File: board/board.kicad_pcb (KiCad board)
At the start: 2 copper layers, 4 parts, among them P2 CONN28

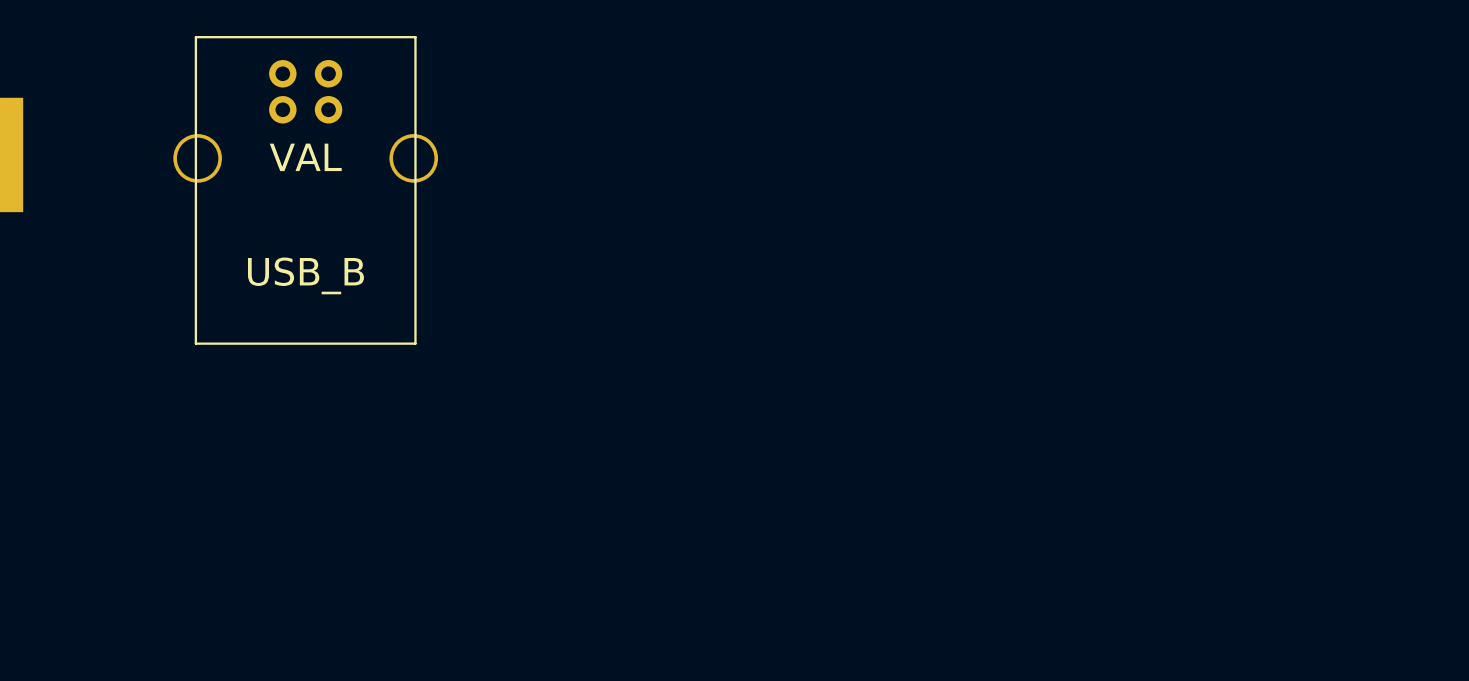
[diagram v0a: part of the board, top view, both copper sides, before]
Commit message: Added some more component outlines.
git-svn-id: http://www.cdkersey.com/log/2015.08.21/eeprom_prog@1664 816618ff-971e-4f3c-9917-b646dc1eeecf
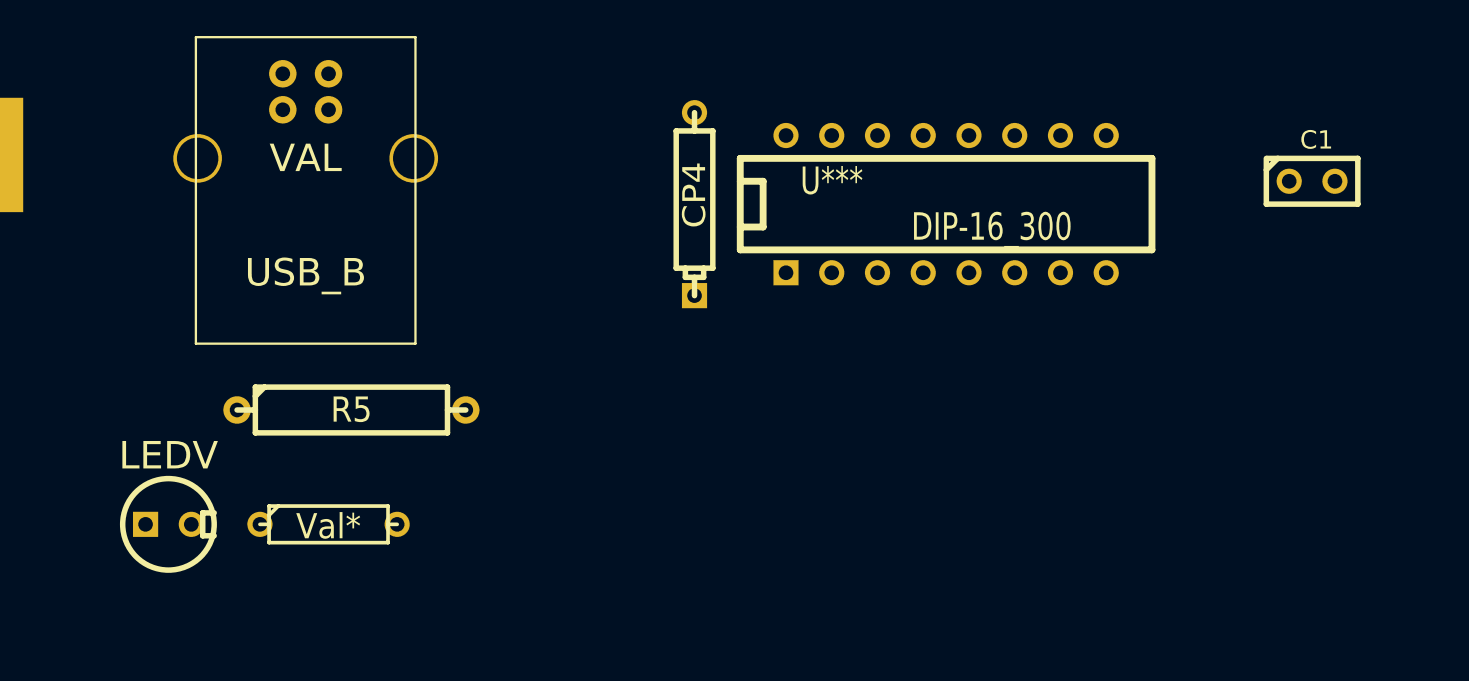
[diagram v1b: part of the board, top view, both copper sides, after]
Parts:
- added C1: V***, C1, F.Cu at (209.6, 77.5)
- added CP4: C***, CP4, F.Cu at (175.3, 78.7)
- added LEDV: D***, LEDV, F.Cu at (146.1, 96.5)
- added R3: Val*, R3, F.Cu at (154.9, 96.5)
- added R5: Val*, R5, F.Cu at (156.2, 90.2)
- added U***: DIP-16_300, DIP-16__300, F.Cu at (189.2, 78.7)
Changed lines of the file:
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@@
     (links 0)
     (no_connects 0)
-    (area 70.616 107.620999 236.549001 180.669001)
+    (area 70.616 69.151499 236.549001 180.669001)
     (thickness 1.6)
     (drawings 0)
     (tracks 0)
     (zones 0)
-    (modules 4)
+    (modules 10)
     (nets 1)
   )
@@
       (rotate (xyz 0 0 0))
     )
+  )
+  (module DIP-16__300 (layer F.Cu)
+    (at 189.23 78.74)
+    (descr "16 pins DIL package, round pads")
+    (tags DIL)
+    (fp_text reference U*** (at -6.35 -1.27) (layer F.SilkS)
+      (effects (font (size 1.524 1.143) (thickness 0.3048)))
+    )
+    (fp_text value DIP-16_300 (at 2.54 1.27) (layer F.SilkS)
+      (effects (font (size 1.524 1.143) (thickness 0.3048)))
+    )
+    (fp_line (start -11.43 -1.27) (end -11.43 -1.27) (layer F.SilkS) (width 0.381))
+    (fp_line (start -11.43 -1.27) (end -10.16 -1.27) (layer F.SilkS) (width 0.381))
+    (fp_line (start -10.16 -1.27) (end -10.16 1.27) (layer F.SilkS) (width 0.381))
+    (fp_line (start -10.16 1.27) (end -11.43 1.27) (layer F.SilkS) (width 0.381))
+    (fp_line (start -11.43 -2.54) (end 11.43 -2.54) (layer F.SilkS) (width 0.381))
+    (fp_line (start 11.43 -2.54) (end 11.43 2.54) (layer F.SilkS) (width 0.381))
+    (fp_line (start 11.43 2.54) (end -11.43 2.54) (layer F.SilkS) (width 0.381))
+    (fp_line (start -11.43 2.54) (end -11.43 -2.54) (layer F.SilkS) (width 0.381))
+    (pad 1 thru_hole rect (at -8.89 3.81) (size 1.397 1.397) (drill 0.8128)
+      (layers *.Cu *.Mask F.SilkS)
+    )
+    (pad 2 thru_hole circle (at -6.35 3.81) (size 1.397 1.397) (drill 0.8128)
+      (layers *.Cu *.Mask F.SilkS)
+    )
+    (pad 3 thru_hole circle (at -3.81 3.81) (size 1.397 1.397) (drill 0.8128)
+      (layers *.Cu *.Mask F.SilkS)
+    )
+    (pad 4 thru_hole circle (at -1.27 3.81) (size 1.397 1.397) (drill 0.8128)
+      (layers *.Cu *.Mask F.SilkS)
+    )
+    (pad 5 thru_hole circle (at 1.27 3.81) (size 1.397 1.397) (drill 0.8128)
+      (layers *.Cu *.Mask F.SilkS)
+    )
+    (pad 6 thru_hole circle (at 3.81 3.81) (size 1.397 1.397) (drill 0.8128)
+      (layers *.Cu *.Mask F.SilkS)
+    )
+    (pad 7 thru_hole circle (at 6.35 3.81) (size 1.397 1.397) (drill 0.8128)
+      (layers *.Cu *.Mask F.SilkS)
+    )
+    (pad 8 thru_hole circle (at 8.89 3.81) (size 1.397 1.397) (drill 0.8128)
+      (layers *.Cu *.Mask F.SilkS)
+    )
+    (pad 9 thru_hole circle (at 8.89 -3.81) (size 1.397 1.397) (drill 0.8128)
+      (layers *.Cu *.Mask F.SilkS)
+    )
+    (pad 10 thru_hole circle (at 6.35 -3.81) (size 1.397 1.397) (drill 0.8128)
+      (layers *.Cu *.Mask F.SilkS)
+    )
+    (pad 11 thru_hole circle (at 3.81 -3.81) (size 1.397 1.397) (drill 0.8128)
+      (layers *.Cu *.Mask F.SilkS)
+    )
+    (pad 12 thru_hole circle (at 1.27 -3.81) (size 1.397 1.397) (drill 0.8128)
+      (layers *.Cu *.Mask F.SilkS)
+    )
+    (pad 13 thru_hole circle (at -1.27 -3.81) (size 1.397 1.397) (drill 0.8128)
+      (layers *.Cu *.Mask F.SilkS)
+    )
+    (pad 14 thru_hole circle (at -3.81 -3.81) (size 1.397 1.397) (drill 0.8128)
+      (layers *.Cu *.Mask F.SilkS)
+    )
+    (pad 15 thru_hole circle (at -6.35 -3.81) (size 1.397 1.397) (drill 0.8128)
+      (layers *.Cu *.Mask F.SilkS)
+    )
+    (pad 16 thru_hole circle (at -8.89 -3.81) (size 1.397 1.397) (drill 0.8128)
+      (layers *.Cu *.Mask F.SilkS)
+    )
+    (model dil/dil_16.wrl
+      (at (xyz 0 0 0))
+      (scale (xyz 1 1 1))
+      (rotate (xyz 0 0 0))
+    )
+  )
+  (module C1 (layer F.Cu)
+    (at 209.55 77.47)
+    (descr "Condensateur e = 1 pas")
+    (tags C)
+    (fp_text reference C1 (at 0.254 -2.286) (layer F.SilkS)
+      (effects (font (size 1.016 1.016) (thickness 0.2032)))
+    )
+    (fp_text value V*** (at 0 -2.286) (layer F.SilkS) hide
+      (effects (font (size 1.016 1.016) (thickness 0.2032)))
+    )
+    (fp_line (start -2.4892 -1.27) (end 2.54 -1.27) (layer F.SilkS) (width 0.3048))
+    (fp_line (start 2.54 -1.27) (end 2.54 1.27) (layer F.SilkS) (width 0.3048))
+    (fp_line (start 2.54 1.27) (end -2.54 1.27) (layer F.SilkS) (width 0.3048))
+    (fp_line (start -2.54 1.27) (end -2.54 -1.27) (layer F.SilkS) (width 0.3048))
+    (fp_line (start -2.54 -0.635) (end -1.905 -1.27) (layer F.SilkS) (width 0.3048))
+    (pad 1 thru_hole circle (at -1.27 0) (size 1.397 1.397) (drill 0.8128)
+      (layers *.Cu *.Mask F.SilkS)
+    )
+    (pad 2 thru_hole circle (at 1.27 0) (size 1.397 1.397) (drill 0.8128)
+      (layers *.Cu *.Mask F.SilkS)
+    )
+    (model discret/capa_1_pas.wrl
+      (at (xyz 0 0 0))
+      (scale (xyz 1 1 1))
+      (rotate (xyz 0 0 0))
+    )
+  )
+  (module CP4 (layer F.Cu)
+    (at 175.26 78.74 90)
+    (descr "Condensateur polarise")
+    (tags CP)
+    (fp_text reference CP4 (at 0.508 0 90) (layer F.SilkS)
+      (effects (font (size 1.27 1.397) (thickness 0.254)))
+    )
+    (fp_text value C*** (at 0.508 0 90) (layer F.SilkS) hide
+      (effects (font (size 1.27 1.143) (thickness 0.254)))
+    )
+    (fp_line (start 5.08 0) (end 4.064 0) (layer F.SilkS) (width 0.3048))
+    (fp_line (start 4.064 0) (end 4.064 1.016) (layer F.SilkS) (width 0.3048))
+    (fp_line (start 4.064 1.016) (end -3.556 1.016) (layer F.SilkS) (width 0.3048))
+    (fp_line (start -3.556 1.016) (end -3.556 -1.016) (layer F.SilkS) (width 0.3048))
+    (fp_line (start -3.556 -1.016) (end 4.064 -1.016) (layer F.SilkS) (width 0.3048))
+    (fp_line (start 4.064 -1.016) (end 4.064 0) (layer F.SilkS) (width 0.3048))
+    (fp_line (start -5.08 0) (end -4.064 0) (layer F.SilkS) (width 0.3048))
+    (fp_line (start -3.556 0.508) (end -4.064 0.508) (layer F.SilkS) (width 0.3048))
+    (fp_line (start -4.064 0.508) (end -4.064 -0.508) (layer F.SilkS) (width 0.3048))
+    (fp_line (start -4.064 -0.508) (end -3.556 -0.508) (layer F.SilkS) (width 0.3048))
+    (pad 1 thru_hole rect (at -5.08 0 90) (size 1.397 1.397) (drill 0.8128)
+      (layers *.Cu *.Mask F.SilkS)
+    )
+    (pad 2 thru_hole circle (at 5.08 0 90) (size 1.397 1.397) (drill 0.8128)
+      (layers *.Cu *.Mask F.SilkS)
+    )
+    (model discret/c_pol.wrl
+      (at (xyz 0 0 0))
+      (scale (xyz 0.4 0.4 0.4))
+      (rotate (xyz 0 0 0))
+    )
+  )
+  (module LEDV (layer F.Cu)
+    (at 146.05 96.52)
+    (descr "Led verticale diam 6mm")
+    (tags "LED DEV")
+    (fp_text reference LEDV (at 0 -3.81) (layer F.SilkS)
+      (effects (font (size 1.524 1.524) (thickness 0.3048)))
+    )
+    (fp_text value D*** (at 0 -3.81) (layer F.SilkS) hide
+      (effects (font (size 1.524 1.524) (thickness 0.3048)))
+    )
+    (fp_circle (center 0 0) (end -2.54 0) (layer F.SilkS) (width 0.3048))
+    (fp_line (start 2.54 -0.635) (end 1.905 -0.635) (layer F.SilkS) (width 0.3048))
+    (fp_line (start 1.905 -0.635) (end 1.905 0.635) (layer F.SilkS) (width 0.3048))
+    (fp_line (start 1.905 0.635) (end 2.54 0.635) (layer F.SilkS) (width 0.3048))
+    (pad 1 thru_hole rect (at -1.27 0) (size 1.397 1.397) (drill 0.8128)
+      (layers *.Cu *.Mask F.SilkS)
+    )
+    (pad 2 thru_hole circle (at 1.27 0) (size 1.397 1.397) (drill 0.8128)
+      (layers *.Cu *.Mask F.SilkS)
+    )
+    (model discret/led5_vertical.wrl
+      (at (xyz 0 0 0))
+      (scale (xyz 1 1 1))
+      (rotate (xyz 0 0 0))
+    )
+  )
+  (module R5 (layer F.Cu)
+    (at 156.21 90.17)
+    (descr "Resistance 5 pas")
+    (tags R)
+    (autoplace_cost180 10)
+    (fp_text reference R5 (at 0 0) (layer F.SilkS)
+      (effects (font (size 1.397 1.27) (thickness 0.2032)))
+    )
+    (fp_text value Val* (at 0 0) (layer F.SilkS) hide
+      (effects (font (size 1.397 1.27) (thickness 0.2032)))
+    )
+    (fp_line (start -6.35 0) (end -5.334 0) (layer F.SilkS) (width 0.3048))
+    (fp_line (start 6.35 0) (end 5.334 0) (layer F.SilkS) (width 0.3048))
+    (fp_line (start 5.334 -1.27) (end 5.334 1.27) (layer F.SilkS) (width 0.3048))
+    (fp_line (start 5.334 1.27) (end -5.334 1.27) (layer F.SilkS) (width 0.3048))
+    (fp_line (start -5.334 1.27) (end -5.334 -1.27) (layer F.SilkS) (width 0.3048))
+    (fp_line (start -5.334 -1.27) (end 5.334 -1.27) (layer F.SilkS) (width 0.3048))
+    (fp_line (start -5.334 -0.762) (end -4.826 -1.27) (layer F.SilkS) (width 0.3048))
+    (pad 1 thru_hole circle (at -6.35 0) (size 1.524 1.524) (drill 0.8128)
+      (layers *.Cu *.Mask F.SilkS)
+    )
+    (pad 2 thru_hole circle (at 6.35 0) (size 1.524 1.524) (drill 0.8128)
+      (layers *.Cu *.Mask F.SilkS)
+    )
+    (model discret/resistor.wrl
+      (at (xyz 0 0 0))
+      (scale (xyz 0.5 0.5 0.5))
+      (rotate (xyz 0 0 0))
+    )
+  )
+  (module R3 (layer F.Cu)
+    (at 154.94 96.52)
+    (descr "Resitance 3 pas")
+    (tags R)
+    (path R3)
+    (autoplace_cost180 10)
+    (fp_text reference R3 (at 0 0.127) (layer F.SilkS) hide
+      (effects (font (size 1.397 1.27) (thickness 0.2032)))
+    )
+    (fp_text value Val* (at 0 0.127) (layer F.SilkS)
+      (effects (font (size 1.397 1.27) (thickness 0.2032)))
+    )
+    (fp_line (start -3.81 0) (end -3.302 0) (layer F.SilkS) (width 0.2032))
+    (fp_line (start 3.81 0) (end 3.302 0) (layer F.SilkS) (width 0.2032))
+    (fp_line (start 3.302 0) (end 3.302 -1.016) (layer F.SilkS) (width 0.2032))
+    (fp_line (start 3.302 -1.016) (end -3.302 -1.016) (layer F.SilkS) (width 0.2032))
+    (fp_line (start -3.302 -1.016) (end -3.302 1.016) (layer F.SilkS) (width 0.2032))
+    (fp_line (start -3.302 1.016) (end 3.302 1.016) (layer F.SilkS) (width 0.2032))
+    (fp_line (start 3.302 1.016) (end 3.302 0) (layer F.SilkS) (width 0.2032))
+    (fp_line (start -3.302 -0.508) (end -2.794 -1.016) (layer F.SilkS) (width 0.2032))
+    (pad 1 thru_hole circle (at -3.81 0) (size 1.397 1.397) (drill 0.8128)
+      (layers *.Cu *.Mask F.SilkS)
+    )
+    (pad 2 thru_hole circle (at 3.81 0) (size 1.397 1.397) (drill 0.8128)
+      (layers *.Cu *.Mask F.SilkS)
+    )
+    (model discret/resistor.wrl
+      (at (xyz 0 0 0))
+      (scale (xyz 0.3 0.3 0.3))
+      (rotate (xyz 0 0 0))
+    )
